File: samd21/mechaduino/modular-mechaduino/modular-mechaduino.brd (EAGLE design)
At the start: 37 x 37 mm, 29 parts, among them J3 CONN_04SCREW_TERM, J4 USB4105-GF-A, J5 CONN_2X4LOCK, U1 UC_ATSAMD21E18AFAB, U2 A4950, U3 A4950, U4 AS5047

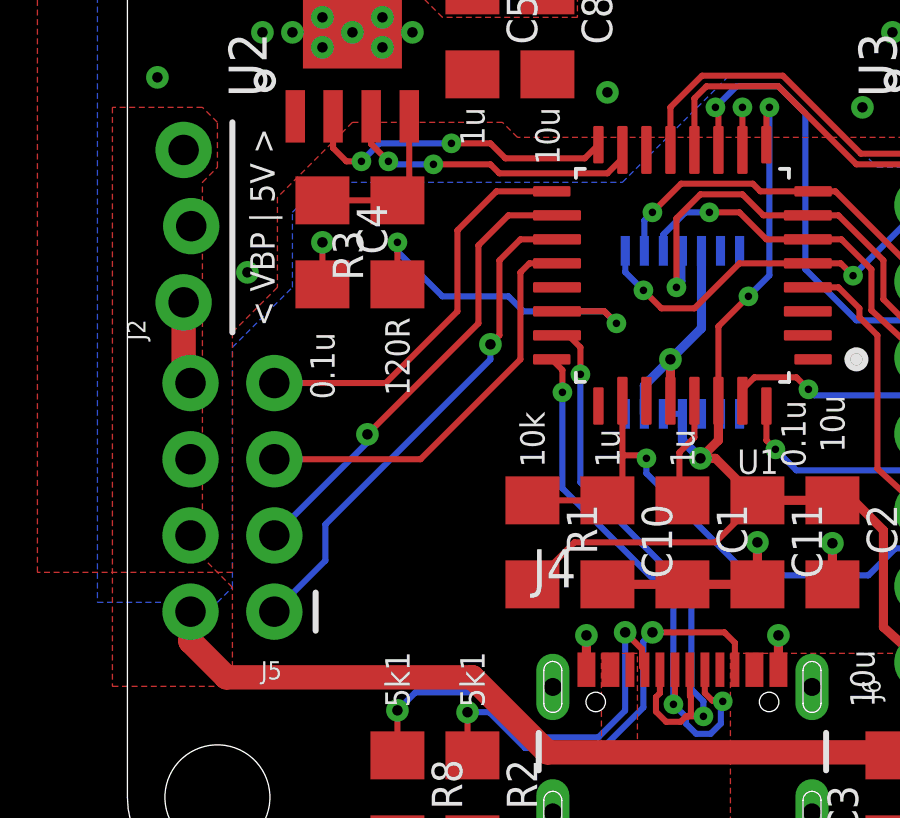
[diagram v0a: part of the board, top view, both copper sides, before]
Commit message: pd hubs differentiated, rm mechaduino ref, add some bus backpacks
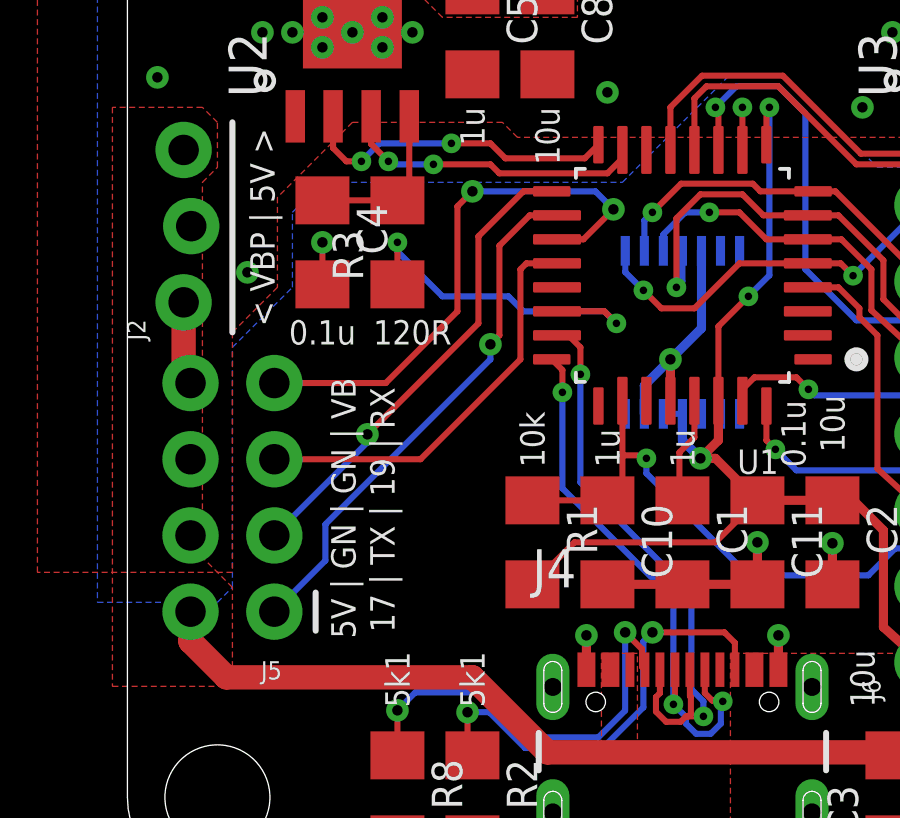
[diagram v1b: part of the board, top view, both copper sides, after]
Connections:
- net PHY_CLK renamed B_PA19
- removed net PHY_CS: J5.7, U1.17
- removed net PHY_MISO: J5.3, U1.18
- removed net PHY_MOSI: J5.1, U1.19
- new net B_PA17: J5.1, U1.18
- new net B_RX: J5.7, U1.19
- new net B_TX: J5.3, U1.17
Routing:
- net B_RX: track 0.00 -> 18.5 mm, vias 0 -> 2
- net B_PA17: track 0.00 -> 17.6 mm, vias 0 -> 1
- net PHY_MOSI: track 17.0 -> 0.00 mm, vias 1 -> 0
- net B_TX: track 0.00 -> 15.9 mm, vias 0 -> 1
- net PHY_MISO: track 15.5 -> 0.00 mm, vias 1 -> 0
- net PHY_CS: track 13.5 -> 0.00 mm
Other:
- board text added: "17 | TX | 19 | RX"
- board text added: "5V | GN | GN | VB"
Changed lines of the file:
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@@
 <setting verticaltext="up"/>
 </settings>
-<grid distance="0.5" unitdist="mm" unit="mm" style="lines" multiple="1" display="yes" altdistance="5" altunitdist="mil" altunit="mil"/>
+<grid distance="0.1" unitdist="mm" unit="mm" style="lines" multiple="1" display="yes" altdistance="5" altunitdist="mil" altunit="mil"/>
 <layers>
 <layer number="1" name="Top" color="4" fill="1" visible="yes" active="yes"/>
@@
 <wire x1="3" y1="0" x2="0" y2="3" width="0" layer="20" curve="-90"/>
 <text x="30" y="19" size="0.8128" layer="21" font="vector" rot="R270" align="center-left">120R</text>
-<text x="9" y="19" size="0.8128" layer="21" font="vector" rot="R270" align="center-left">120R</text>
-<text x="6.5" y="18.5" size="0.8128" layer="21" font="vector" rot="R270" align="center-left">0.1u</text>
+<text x="9.5" y="18.5" size="0.8128" layer="21" font="vector" align="center">120R</text>
+<text x="6.5" y="18.5" size="0.8128" layer="21" font="vector" align="center">0.1u</text>
 <text x="35" y="25.5" size="0.8128" layer="21" font="vector" rot="R270" align="center-left">10u</text>
 <text x="32.5" y="25.5" size="0.8128" layer="21" font="vector" rot="R270" align="center-left">1u</text>
@@
 <text x="34" y="18.5" size="1.016" layer="22" font="vector" rot="MR270" align="center">"forever diddling drawings
 of trivial mechanisms"</text>
+<text x="7.2" y="8.3" size="0.8128" layer="21" font="vector" rot="R90" align="center-left">5V | GN | GN | VB</text>
+<text x="8.5" y="8.5" size="0.8128" layer="21" font="vector" rot="R90" align="center-left">17 | TX | 19 | RX</text>
 </plain>
 <attributes>
@@
 <wire x1="14.18" y1="2.5" x2="14.18" y2="6.68" width="0" layer="19" extent="1-1"/>
 </signal>
-<signal name="PHY_MOSI">
-<contactref element="J5" pad="1"/>
-<contactref element="U1" pad="19"/>
-<wire x1="6.6" y1="10.893" x2="4.897" y2="9.19" width="0.2032" layer="16"/>
-<wire x1="14.32" y1="21.6" x2="13.1" y2="21.6" width="0.2032" layer="1"/>
-<wire x1="12.4" y1="18.4" x2="12.1" y2="18.1" width="0.2032" layer="1"/>
-<via x="12.1" y="18.1" extent="1-16" drill="0.35"/>
-<wire x1="12.1" y1="18.1" x2="12.1" y2="17.6" width="0.2032" layer="16"/>
-<wire x1="12.1" y1="17.6" x2="6.6" y2="12.1" width="0.2032" layer="16"/>
-<wire x1="13.1" y1="21.6" x2="12.4" y2="20.9" width="0.2032" layer="1"/>
-<wire x1="12.4" y1="20.9" x2="12.4" y2="18.4" width="0.2032" layer="1"/>
-<wire x1="6.6" y1="12.1" x2="6.6" y2="10.893" width="0.2032" layer="16"/>
-</signal>
-<signal name="PHY_MISO">
-<contactref element="J5" pad="3"/>
-<contactref element="U1" pad="18"/>
-<wire x1="4.897" y1="11.73" x2="8" y2="14.833" width="0.2032" layer="16"/>
-<wire x1="8" y1="14.833" x2="8" y2="15.1" width="0.2032" layer="16"/>
-<via x="8" y="15.1" extent="1-16" drill="0.35"/>
-<wire x1="12.7" y1="22.4" x2="14.32" y2="22.4" width="0.2032" layer="1"/>
-<wire x1="8" y1="15.1" x2="11.7" y2="18.8" width="0.2032" layer="1"/>
-<wire x1="11.7" y1="18.8" x2="11.7" y2="21.4" width="0.2032" layer="1"/>
-<wire x1="11.7" y1="21.4" x2="12.7" y2="22.4" width="0.2032" layer="1"/>
-</signal>
-<signal name="PHY_CLK">
-<contactref element="J5" pad="5"/>
-<contactref element="U1" pad="20"/>
-<wire x1="14.32" y1="20.8" x2="13.4" y2="20.8" width="0.2032" layer="1"/>
-<wire x1="13.1" y1="20.5" x2="13.1" y2="17.6" width="0.2032" layer="1"/>
-<wire x1="13.1" y1="17.6" x2="9.77" y2="14.27" width="0.2032" layer="1"/>
-<wire x1="9.77" y1="14.27" x2="4.897" y2="14.27" width="0.2032" layer="1"/>
-<wire x1="13.4" y1="20.8" x2="13.1" y2="20.5" width="0.2032" layer="1"/>
-</signal>
-<signal name="PHY_CS">
-<contactref element="J5" pad="7"/>
-<contactref element="U1" pad="17"/>
-<wire x1="4.897" y1="16.81" x2="8.61" y2="16.81" width="0.2032" layer="1"/>
-<wire x1="12.3" y1="23.2" x2="14.145" y2="23.2" width="0.2032" layer="1"/>
-<wire x1="8.61" y1="16.81" x2="11" y2="19.2" width="0.2032" layer="1"/>
-<wire x1="11" y1="19.2" x2="11" y2="21.9" width="0.2032" layer="1"/>
-<wire x1="11" y1="21.9" x2="12.3" y2="23.2" width="0.2032" layer="1"/>
-</signal>
 <signal name="N$10">
 <contactref element="J5" pad="8"/>
@@
 <wire x1="1.873" y1="17.04" x2="1.873" y2="19.5" width="0.8128" layer="1"/>
 </signal>
+<signal name="B_TX">
+<contactref element="U1" pad="17"/>
+<contactref element="J5" pad="3"/>
+<wire x1="4.897" y1="11.73" x2="8" y2="14.833" width="0.2032" layer="16"/>
+<wire x1="8" y1="14.833" x2="8" y2="15.1" width="0.2032" layer="16"/>
+<via x="8" y="15.1" extent="1-16" drill="0.35"/>
+<wire x1="8" y1="15.1" x2="11.7" y2="18.8" width="0.2032" layer="1"/>
+<wire x1="11.7" y1="18.8" x2="11.7" y2="21.7" width="0.2032" layer="1"/>
+<wire x1="13.2" y1="23.2" x2="14.145" y2="23.2" width="0.2032" layer="1"/>
+<wire x1="11.7" y1="21.7" x2="13.2" y2="23.2" width="0.2032" layer="1"/>
+</signal>
+<signal name="B_PA17">
+<contactref element="U1" pad="18"/>
+<contactref element="J5" pad="1"/>
+<wire x1="6.6" y1="10.893" x2="4.897" y2="9.19" width="0.2032" layer="16"/>
+<wire x1="12.4" y1="18.4" x2="12.1" y2="18.1" width="0.2032" layer="1"/>
+<via x="12.1" y="18.1" extent="1-16" drill="0.35"/>
+<wire x1="12.1" y1="18.1" x2="12.1" y2="17.6" width="0.2032" layer="16"/>
+<wire x1="12.1" y1="17.6" x2="6.6" y2="12.1" width="0.2032" layer="16"/>
+<wire x1="12.4" y1="21.38858125" x2="12.4" y2="18.4" width="0.2032" layer="1"/>
+<wire x1="6.6" y1="12.1" x2="6.6" y2="10.893" width="0.2032" layer="16"/>
+<wire x1="13.41141875" y1="22.4" x2="14.32" y2="22.4" width="0.2032" layer="1"/>
+<wire x1="12.4" y1="21.38858125" x2="13.41141875" y2="22.4" width="0.2032" layer="1"/>
+</signal>
+<signal name="B_RX">
+<contactref element="U1" pad="19"/>
+<contactref element="J5" pad="7"/>
+<wire x1="4.897" y1="16.81" x2="8.61" y2="16.81" width="0.2032" layer="1"/>
+<wire x1="8.61" y1="16.81" x2="11" y2="19.2" width="0.2032" layer="1"/>
+<wire x1="11" y1="19.2" x2="11" y2="22.7" width="0.2032" layer="1"/>
+<wire x1="11" y1="22.7" x2="11.5" y2="23.2" width="0.2032" layer="1"/>
+<wire x1="14.32" y1="21.6" x2="15.2" y2="21.6" width="0.2032" layer="1"/>
+<wire x1="15.2" y1="21.6" x2="16.2" y2="22.6" width="0.2032" layer="1"/>
+<via x="16.2" y="22.6" extent="1-16" drill="0.35"/>
+<wire x1="16.2" y1="22.6" x2="15.6" y2="23.2" width="0.2032" layer="16"/>
+<via x="11.5" y="23.2" extent="1-16" drill="0.35"/>
+<wire x1="15.6" y1="23.2" x2="11.5" y2="23.2" width="0.2032" layer="16"/>
+</signal>
+<signal name="B_PA19">
+<contactref element="U1" pad="20"/>
+<contactref element="J5" pad="5"/>
+<wire x1="13.1" y1="20.6" x2="13.1" y2="17.6" width="0.2032" layer="1"/>
+<wire x1="13.1" y1="17.6" x2="9.77" y2="14.27" width="0.2032" layer="1"/>
+<wire x1="9.77" y1="14.27" x2="4.897" y2="14.27" width="0.2032" layer="1"/>
+<wire x1="13.3" y1="20.8" x2="13.1" y2="20.6" width="0.2032" layer="1"/>
+<wire x1="14.32" y1="20.8" x2="13.3" y2="20.8" width="0.2032" layer="1"/>
+</signal>
 </signals>
